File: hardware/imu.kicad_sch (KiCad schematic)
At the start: 5 parts, among them U3 ICM-42688-P

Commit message: feat(kicad): Cleared ERC errors and assigned footprints for all parts
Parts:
- C17, C18, C19: footprint Capacitor_SMD:C_0603_1608Metric -> Capacitor_SMD:C_0402_1005Metric
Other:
- note added: "Application Notes 1) 0.1uF => X7R, +- 10% 2) 2.2uF => X7R, +- 10% 3) 10nF => X7R, +- 10%"
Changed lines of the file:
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@@
+		)
+	)
+	(text "Application Notes\n1) 0.1uF => X7R, +- 10%\n2) 2.2uF => X7R, +- 10%\n3) 10nF => X7R, +- 10%"
+		(exclude_from_sim no)
+		(at 98.044 109.22 0)
+		(effects
+			(font
+				(size 1.27 1.27)
+			)
+			(justify left)
 		)
 	)
@@
 			)
 		)
-		(property "Footprint" "Capacitor_SMD:C_0603_1608Metric"
+		(property "Footprint" "Capacitor_SMD:C_0402_1005Metric"
 			(at 183.8452 80.01 0)
 			(hide yes)
@@
 			)
 		)
-		(property "Footprint" "Capacitor_SMD:C_0603_1608Metric"
+		(property "Footprint" "Capacitor_SMD:C_0402_1005Metric"
 			(at 190.1952 80.01 0)
 			(hide yes)
@@
 			)
 		)
-		(property "Footprint" "Capacitor_SMD:C_0603_1608Metric"
+		(property "Footprint" "Capacitor_SMD:C_0402_1005Metric"
 			(at 177.4952 80.01 0)
 			(hide yes)

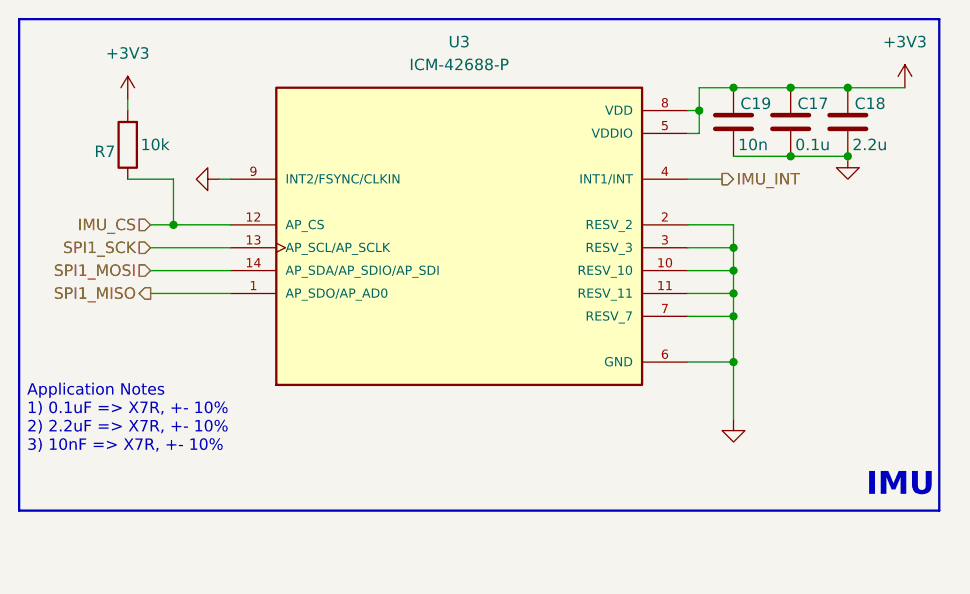
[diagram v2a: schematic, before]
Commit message: feat(kicad): Added application notes for the IMU
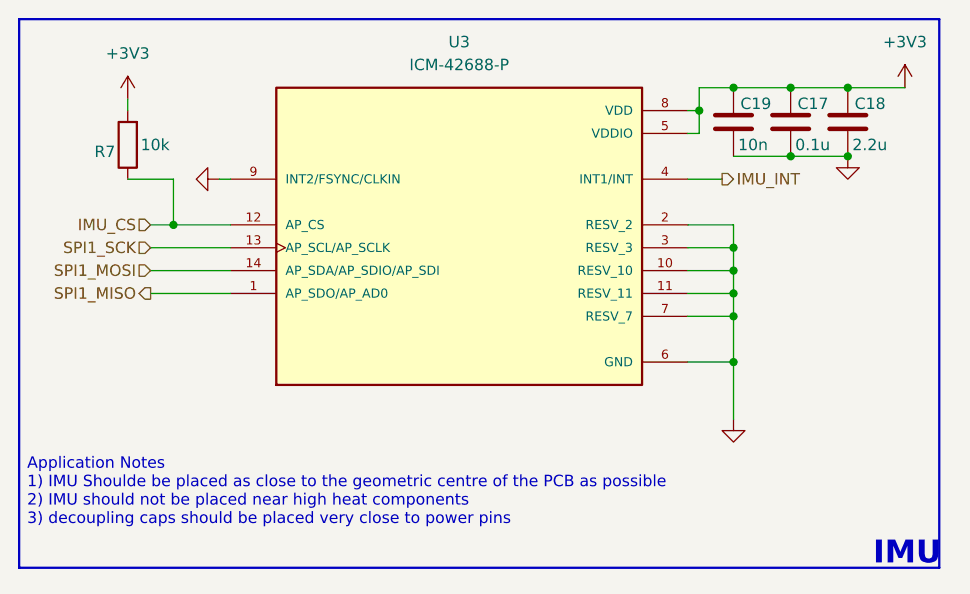
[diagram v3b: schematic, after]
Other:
- note added: "Application Notes 1) IMU Shoulde be placed as close to the geometric centre of the PCB as possible 2) IMU should not be placed near high heat components 3) decoupling caps should be placed very close to power pins"
- note removed: "Application Notes 1) 0.1uF => X7R, +- 10% 2) 2.2uF => X7R, +- 10% 3) 10nF => X7R, +- 10%"
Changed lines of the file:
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@@
 	(rectangle
 		(start 97.155 64.77)
-		(end 199.39 119.38)
+		(end 199.39 125.73)
 		(stroke
 			(width 0.254)
@@
 		)
 	)
-	(text "Application Notes\n1) 0.1uF => X7R, +- 10%\n2) 2.2uF => X7R, +- 10%\n3) 10nF => X7R, +- 10%"
+	(text "Application Notes\n1) IMU Shoulde be placed as close to the geometric centre of the PCB as possible\n2) IMU should not be placed near high heat components\n3) decoupling caps should be placed very close to power pins\n"
 		(exclude_from_sim no)
-		(at 98.044 109.22 0)
+		(at 98.044 117.348 0)
 		(effects
 			(font
@@
 	(text "IMU\n"
 		(exclude_from_sim no)
-		(at 195.072 116.586 0)
+		(at 195.834 124.206 0)
 		(effects
 			(font

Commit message: feat(kicad): Routing complete, assigning jlc components to each footprint
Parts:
- C17: value 0.1u -> 100n; LCSC (none) -> C1525
- C18: value 2.2u -> 2u2
- R7: LCSC (none) -> C25744
- U3: LCSC (none) -> C1850418
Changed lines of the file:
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@@
 			)
 		)
-		(property "Value" "0.1u"
+		(property "Value" "100n"
 			(at 183.388 78.74 0)
 			(show_name no)
@@
 		)
 		(property "Description" "Unpolarized capacitor"
+			(at 182.88 76.2 0)
+			(hide yes)
+			(show_name no)
+			(do_not_autoplace no)
+			(effects
+				(font
+					(size 1.27 1.27)
+				)
+			)
+		)
+		(property "LCSC" "C1525"
+			(at 182.88 76.2 0)
+			(hide yes)
+			(show_name no)
+			(do_not_autoplace no)
+			(effects
+				(font
+					(size 1.27 1.27)
+				)
+			)
+		)
+		(property "KLC_S3.3" ""
+			(at 182.88 76.2 0)
+			(hide yes)
+			(show_name no)
+			(do_not_autoplace no)
+			(effects
+				(font
+					(size 1.27 1.27)
+				)
+			)
+		)
+		(property "KLC_S4.1" ""
 			(at 182.88 76.2 0)
 			(hide yes)
@@
 			)
 		)
-		(property "Value" "2.2u"
+		(property "Value" "2u2"
 			(at 189.738 78.74 0)
 			(show_name no)
@@
 		)
 		(property "Description" "Unpolarized capacitor"
+			(at 189.23 76.2 0)
+			(hide yes)
+			(show_name no)
+			(do_not_autoplace no)
+			(effects
+				(font
+					(size 1.27 1.27)
+				)
+			)
+		)
+		(property "LCSC" ""
+			(at 189.23 76.2 0)
+			(hide yes)
+			(show_name no)
+			(do_not_autoplace no)
+			(effects
+				(font
+					(size 1.27 1.27)
+				)
+			)
+		)
+		(property "KLC_S3.3" ""
+			(at 189.23 76.2 0)
+			(hide yes)
+			(show_name no)
+			(do_not_autoplace no)
+			(effects
+				(font
+					(size 1.27 1.27)
+				)
+			)
+		)
+		(property "KLC_S4.1" ""
 			(at 189.23 76.2 0)
 			(hide yes)
@@
 		)
 		(property "Description" "Unpolarized capacitor"
+			(at 176.53 76.2 0)
+			(hide yes)
+			(show_name no)
+			(do_not_autoplace no)
+			(effects
+				(font
+					(size 1.27 1.27)
+				)
+			)
+		)
+		(property "LCSC" ""
+			(at 176.53 76.2 0)
+			(hide yes)
+			(show_name no)
+			(do_not_autoplace no)
+			(effects
+				(font
+					(size 1.27 1.27)
+				)
+			)
+		)
+		(property "KLC_S3.3" ""
+			(at 176.53 76.2 0)
+			(hide yes)
+			(show_name no)
+			(do_not_autoplace no)
+			(effects
+				(font
+					(size 1.27 1.27)
+				)
+			)
+		)
+		(property "KLC_S4.1" ""
 			(at 176.53 76.2 0)
 			(hide yes)
@@
 			)
 		)
+		(property "LCSC" "C1850418"
+			(at 146.05 87.63 0)
+			(hide yes)
+			(show_name no)
+			(do_not_autoplace no)
+			(effects
+				(font
+					(size 1.27 1.27)
+				)
+			)
+		)
+		(property "KLC_S3.3" ""
+			(at 146.05 87.63 0)
+			(hide yes)
+			(show_name no)
+			(do_not_autoplace no)
+			(effects
+				(font
+					(size 1.27 1.27)
+				)
+			)
+		)
+		(property "KLC_S4.1" ""
+			(at 146.05 87.63 0)
+			(hide yes)
+			(show_name no)
+			(do_not_autoplace no)
+			(effects
+				(font
+					(size 1.27 1.27)
+				)
+			)
+		)
 		(pin "2"
 		)
@@
 			(at 109.22 78.74 0)
 			(hide yes)
+			(show_name no)
+			(do_not_autoplace no)
+			(effects
+				(font
+					(size 1.27 1.27)
+				)
+			)
+		)
+		(property "LCSC" "C25744"
+			(at 109.22 78.74 0)
+			(hide yes)
+			(show_name no)
+			(do_not_autoplace no)
+			(effects
+				(font
+					(size 1.27 1.27)
+				)
+			)
+		)
+		(property "KLC_S3.3" ""
+			(at 109.22 78.74 0)
+			(hide yes)
+			(show_name no)
+			(do_not_autoplace no)
+			(effects
+				(font
+					(size 1.27 1.27)
+				)
+			)
+		)
+		(property "KLC_S4.1" ""
+			(at 109.22 78.74 0)
+			(hide yes)

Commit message: feat(kicad): Cleaned up routing and picked LCSC parts for several components
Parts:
- C18: LCSC (none) -> C12530
- C19: LCSC (none) -> C15195
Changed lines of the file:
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@@
 			)
 		)
-		(property "LCSC" ""
+		(property "LCSC" "C12530"
 			(at 189.23 76.2 0)
 			(hide yes)
@@
 			)
 		)
-		(property "LCSC" ""
+		(property "LCSC" "C15195"
 			(at 176.53 76.2 0)
 			(hide yes)
